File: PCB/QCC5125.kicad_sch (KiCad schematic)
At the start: 11 parts, among them J3 BT1 Ant, J4 BT_usb, U16 BTM525

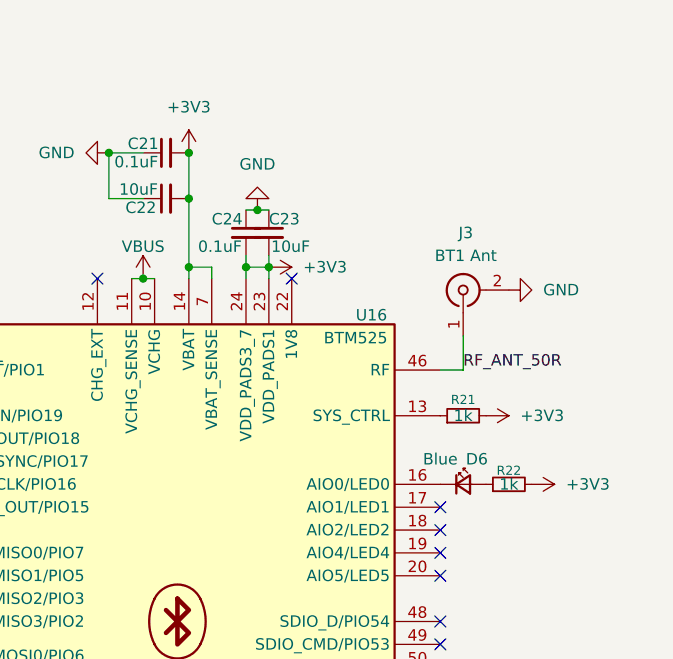
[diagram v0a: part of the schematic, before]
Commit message: updated schematics
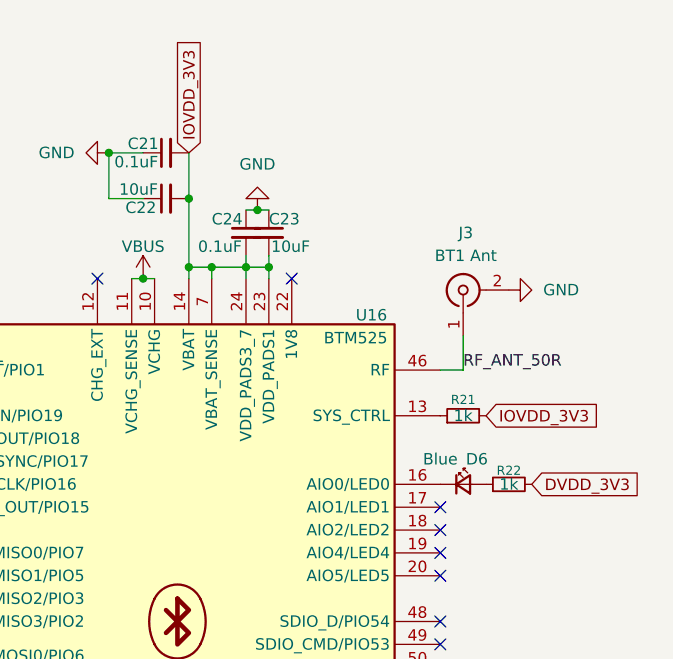
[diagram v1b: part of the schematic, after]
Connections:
- net +3V3 renamed IOVDD_3V3
- net IOVDD_3V3: no longer R22.2
- new net DVDD_3V3: R22.2
